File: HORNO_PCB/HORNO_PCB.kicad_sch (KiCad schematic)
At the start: 104 parts, among them J0_1 Alimentacion dispositivo seri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, J0_10 Terminales de tornillo espaci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, J0_11 Terminales de tornillo espaci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, J0_12 Terminales de tornillo espaci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, J0_13 Terminales de tornillo espaci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, J0_14 Terminales de tornillo espaci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, J0_15 Terminales de tornillo espaci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, J0_18 Terminales de tornillo espaci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, J0_2 Terminales de tornillo espaci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, J0_3 Terminales de tornillo espaci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, J0_4 Terminales de tornillo espaci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, J0_5 Terminales de tornillo espaci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, J0_6 Terminales de tornillo espaci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, J0_7 Terminales de tornillo espaci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, J0_8 Terminales de tornillo espaci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, J0_9 Terminales de tornillo espaci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, J1 +5V +24V, J10 switch, J11 switch, J12 switch, J13 switch, J14 switch, J15 switch, J16 switch, J17 switch, J18 switch, J19 switch, J20 switch, J21 switch, J22 switch, J23 switch, J24 Screw_Terminal_01x20, J25 Screw_Terminal_01x20, J26 Screw_Terminal_01x20, J27 Screw_Terminal_01x20, J7 24VDC, J8 switch, J9 switch, K1 Relay 1, K2 Relay 2, K6 Relay 4, K7 Relay 3, K8 Relay 2, K9 Relay 1, Q1 2N2222, Q2 2N2222, Q6 IRG4PF50W, Q7 IRG4PF50W, U1 TLP521-1, U10 LM741, U15 TLP250, U17 LM741, U18 LM741, U19 TLP250, U2 TLP521-1, U25 UDN2981A, U3 TLP521-1, U4 TLP521-1, U9 LM741

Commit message: Check point 1
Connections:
- net at R1.2, R2.2, R3.2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: now also J13.1 (Pin_1), J26.11 (Pin_11), J26.17 (Pin_17), J26.5 (Pin_5), Q1.3 (C), Q2.3 (C); no longer J11.1 (Pin_1), J21.1 (Pin_1), J24.2 (Pin_2), J25.19 (Pin_19)
- net at C10.2, C5.2, C6.2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: now also J14.1 (Pin_1); no longer J0_5.3 (Pin_3), J15.1 (Pin_1), J22.1 (Pin_1)
- net at U10.4 (V-), U15.5 (VEE), U17.4 (V-)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: now also J15.1 (Pin_1); no longer J14.1 (Pin_1)
- net at D10.2 (A), D11.2 (A), D12.2 (A)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: now also J19.1 (Pin_1), J21.1 (Pin_1); no longer J23.1 (Pin_1)
- new net: J11.1 (Pin_1), J24.2 (Pin_2), J25.19 (Pin_19)
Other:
- note added: "-12 VDC"
- note added: "Dispositivo serial"
- note removed: "VERIFICAR SE SE NECESITA UN CONECTOR MAS PARA LA ALIMENTACION CONFIRMAR EL TIPO DE CONECTOR"
- moved on the sheet: J10, J11, J13, J14, J16, J17, J18, J19, J21, J22, J23, J8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

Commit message: Check point 2
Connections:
- net at C10.2, C5.2, C6.2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: now also J0_5.3 (Pin_3)
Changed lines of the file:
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@@
+	)
+	(junction
+		(at 1112.52 355.6)
+		(diameter 0)
+		(color 0 0 0 0)
 	)
 	(junction
@@
 	(wire
 		(pts
-			(xy 1112.52 309.88) (xy 1112.52 373.38)
+			(xy 1112.52 309.88) (xy 1112.52 355.6)
 		)
 		(stroke
@@
 	(wire
 		(pts
+			(xy 1112.52 355.6) (xy 1112.52 373.38)
+		)
+		(stroke
+			(width 0)
+			(type default)
+			(color 0 0 0 1)
+		)
+	)
+	(wire
+		(pts
 			(xy 514.35 541.02) (xy 514.35 554.99)
 		)
@@
 		)
 	)
+	(wire
+		(pts
+			(xy 1112.52 355.6) (xy 1127.76 355.6)
+		)
+		(stroke
+			(width 0)
+			(type default)
+			(color 0 0 0 1)
+		)
+	)

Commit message: Diseño del PCB: finalizado
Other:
- note added: "RX"
- note added: "TX"
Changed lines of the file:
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@@
+		)
+	)
+	(text "TX"
+		(exclude_from_sim no)
+		(at 468.122 103.378 0)
+		(effects
+			(font
+				(size 1.5748 1.5748)
+			)
 		)
 	)
@@
 			)
 		)
+	)
+	(text "RX"
+		(exclude_from_sim no)
+		(at 471.932 103.124 0)
+		(effects
+			(font
+				(size 1.5748 1.5748)
+			)
+		)

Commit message: Codigo de prueba (pendiente la correccion a la PCB
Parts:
- added R13, R16, R17, R18, R27, R29: Depende de la aplicación salida analógica, Resistor_THT:R_Axial_DIN0207_L6.3mm_D2.5mm_P10.16mm_Horizontal, symbol Device:R_US
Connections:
- net at C10.2, C5.2, C6.2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: now also D10.1 (K), D11.1 (K), D12.1 (K), D13.1 (K), D14.1 (K), D9.1 (K), K1.A2, K2.A2, K6.A2, K7.A2, K8.A2, K9.A2
- net at K9.A1, U25.15 (O4): now also R17.2; no longer D12.1 (K)
- net at K1.A1, U25.13 (O6): now also R13.2; no longer D14.1 (K)
- net at K2.A1, U25.14 (O5): now also R16.2; no longer D13.1 (K)
- net at K6.A1, U25.18 (O1): now also R29.2; no longer D9.1 (K)
- net at K8.A1, U25.16 (O3): now also R18.2; no longer D11.1 (K)
- net at K7.A1, U25.17 (O2): now also R27.2; no longer D10.1 (K)
- new net: F1.1, J0_11.3 (Pin_3), J0_12.3 (Pin_3), J0_15.3 (Pin_3), J0_2.3 (Pin_3), J17.1 (Pin_1), J19.1 (Pin_1), J21.1 (Pin_1)
- new net: D12.2 (A), R17.1
- new net: D13.2 (A), R16.1
- new net: D9.2 (A), R29.1
- new net: D14.2 (A), R13.1
- new net: D11.2 (A), R18.1
- new net: D10.2 (A), R27.1
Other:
- moved on the sheet: D10, D11, D12, D13, D14, D9

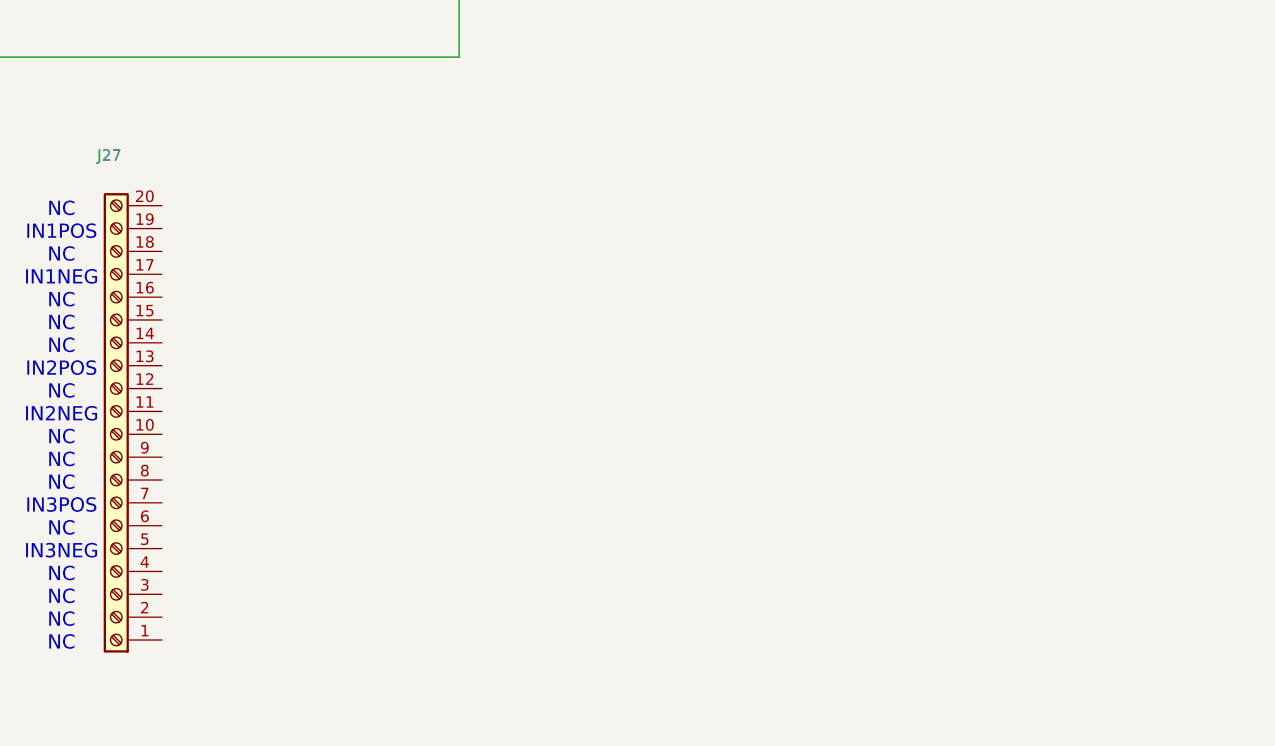
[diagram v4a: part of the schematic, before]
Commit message: Correccion de esquematico y PCB
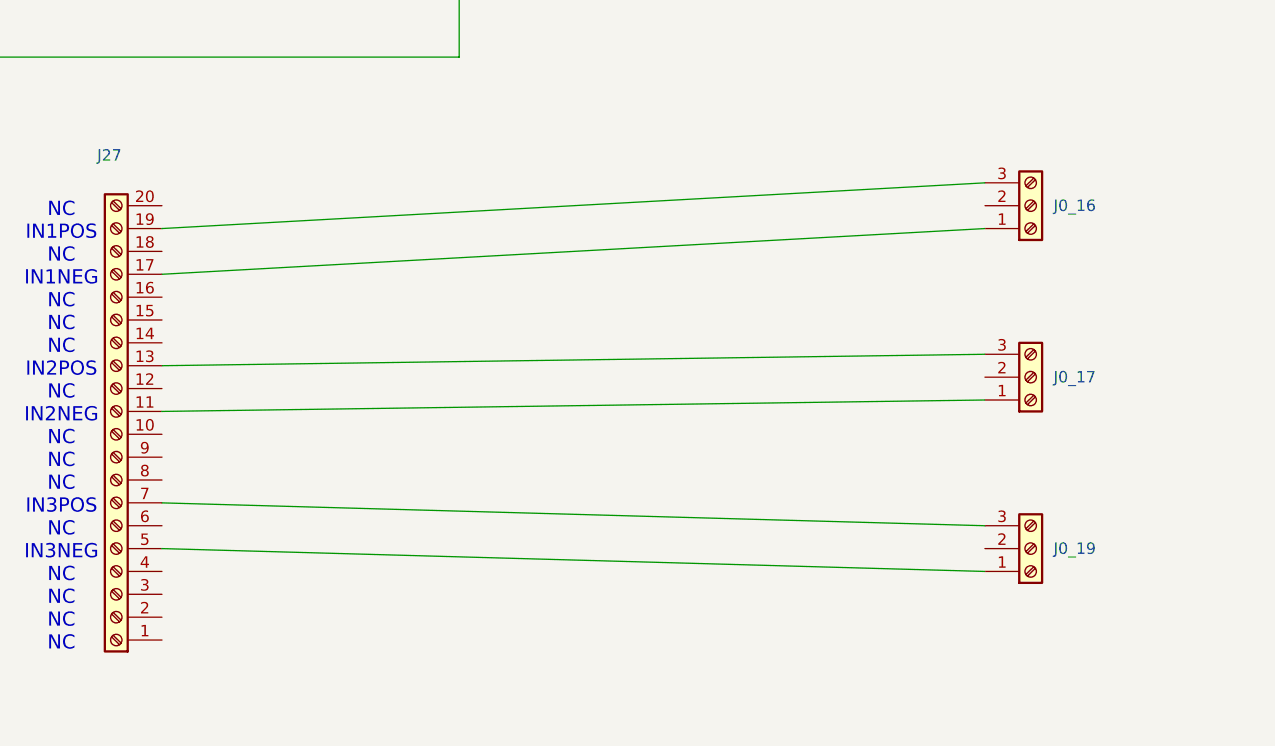
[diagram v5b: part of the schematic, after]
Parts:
- added J0_16, J0_17, J0_19: Terminales de tornillo espaciados en 5mm, TerminalBlock_Phoenix:TerminalBlock_Phoenix_PT-1,5-3-5.0-H_1x03_P5.00mm_Horizontal, symbol Connector:Screw_Terminal_01x03
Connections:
- net at J27.11 (Pin_11): now also J0_17.1 (Pin_1)
- net at J27.13 (Pin_13): now also J0_17.3 (Pin_3)
- net at J27.17 (Pin_17): now also J0_16.1 (Pin_1)
- net at J27.19 (Pin_19): now also J0_16.3 (Pin_3)
- net at J27.5 (Pin_5): now also J0_19.1 (Pin_1)
- net at J27.7 (Pin_7): now also J0_19.3 (Pin_3)

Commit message: PCB corregida
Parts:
- removed J10, J11, J12, J13, J14, J15, J16, J17, J18, J19, J20, J21, J22, J23, J8, J9: switch, TerminalBlock_MetzConnect:TerminalBlock_MetzConnect_360271_1x01_Horizontal_ScrewM3.0_Boxed, symbol Connector:Screw_Terminal_01x01
- removed K6: Relay 4, Relay_THT:Relay_SPDT_Fujitsu_FTR-LYCA005x_FormC_Vertical, symbol Relay:SANYOU_SRD_Form_C
- added Fuente_1: 12VDC, Fuente_step:step_source, symbol Fuente_step:step_source
- added Fuente_2: 5VDC, Fuente_step:step_source, symbol Fuente_step:step_source
- added Fuente_3: 3.3VDC, Fuente_step:step_source, symbol Fuente_step:step_source
- added Fuente_4: -12VDC, Fuente_step:step_source, symbol Fuente_step:step_source
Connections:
- net at J24.2 (Pin_2), J25.19 (Pin_19): now also Fuente_2.4 (OUT+)
- net at C10.2, C5.2, C6.2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: now also J0_10.3 (Pin_3), Fuente_1.2 (IN-), Fuente_1.3 (OUT-), Fuente_2.2 (IN-), Fuente_2.3 (OUT-), Fuente_3.2 (IN-), Fuente_3.3 (OUT-), Fuente_4.3 (OUT-)
- net at U10.4 (V-), U15.5 (VEE), U17.4 (V-)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: now also Fuente_4.4 (OUT+)
- net at U10.7 (V+), U15.8 (VCC), U17.7 (V+)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: now also Fuente_1.4 (OUT+)
- net at F1.1, J0_11.3 (Pin_3), J0_12.3 (Pin_3)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: now also Fuente_1.1 (IN+), Fuente_2.1 (IN+), Fuente_3.1 (IN+)
- net at J0_10.1 (Pin_1): now also R29.2, R48.1
- net at J26.11 (Pin_11), J26.17 (Pin_17), J26.5 (Pin_5)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: now also Fuente_3.4 (OUT+)
- net at U25.18 (O1): no longer R29.2
- net at U25.1 (I1): no longer R48.1
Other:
- note removed: "-12 VDC"
- note removed: "12 VDC"
- note removed: "Fuente step-down"
